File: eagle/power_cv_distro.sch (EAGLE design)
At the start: 54 parts, among them U1 POWER, U10 TLV2372IP, U11 TLV2372IP, U12 TLV2372IP, U13 TLV2372IP, U2 POWER, U3 POWER, U4 POWER, U5 POWER, U6 POWER, U7 POWER, U8 POWER, U9 POWER

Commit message: power dist do-over begins
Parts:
- removed C1, C2, C3, C4: 100n, rcl:C-US025-025X050
- removed C5: 10u, rcl:CPOL-USB45181A
- removed C8: 100n, rcl:C-US050-024X044
- removed JP2, JP3: (no value), pinhead:PINHD-1X8
- removed R1, R10, R13, R14, R2, R5, R6, R7: 1k8, rcl:R-US_0204/2V
- removed R11, R12, R15, R16, R17, R18, R19, R20, R21, R22, R23, R24, R25, R26, R27, R28, R29, R3, R30, R31, R32, R4, R8, R9: 1k, rcl:R-US_0207/7
- removed U$2: FB, adafruit:FB
- added D1, D10, D11, D12, D13, D14, D15, D16, D17, D18, D19, D2, D20, D21, D22, D23, D24, D3, D4, D5, D6, D7, D8, D9: 1N4148DO35-7, TR808clone:1N4148DO35-7
- added X3, X4: (no value), con-molex:22-23-2061
- U10, U11, U12, U13: value TLV2372IP -> POWER; device Texas Instruments_By_element14_Batch_1:TLV2372IP -> eurorack:POWER
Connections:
- removed net N$37: R22.1, U1.GATE
- removed net N$38: R21.1, U1.CV
- removed net N$39: R23.1, U2.GATE
- removed net N$40: R24.1, U2.CV
- removed net N$41: R25.1, U3.GATE
- removed net N$42: R26.1, U3.CV
- removed net N$43: R27.1, U7.GATE
- removed net N$44: R28.1, U7.CV
- removed net N$45: R29.1, U4.GATE
- removed net N$46: R30.1, U4.CV
- removed net N$47: R31.1, U8.GATE
- removed net N$48: R32.1, U8.CV
- removed net VDD: C1.1, C2.1, C3.1, C4.1, C5.+, C8.1, U$2.2, U10.VDD, U11.VDD, U12.VDD, U13.VDD
- net +12V: no longer U$2.1
- net +5V: now also D10.A, D11.A, D12.A, D19.A, D20.A, D21.A, D22.A, D23.A, D24.A, D7.A, D8.A, D9.A, U10.+5V, U11.+5V, U12.+5V, U13.+5V
- net -12V: now also U10.-12V, U11.-12V, U12.-12V, U13.-12V
- net GND: no longer C1.2, C2.2, C3.2, C4.2, C5.-, C8.2, R11.1, R12.1, R15.1, R16.1, R3.1, R4.1, R8.1, R9.1
- net N$1: now also D1.A, X3-1.S; no longer JP2.8, R17.2
- net N$10: now also D4.C, U2.CV; no longer JP3.7, U12.1IN_+
- net N$11: now also D5.C, U3.CV; no longer JP3.6, R27.2
- net N$12: now also D6.C, U7.CV; no longer JP3.5, U12.2IN+
- net N$13: now also D7.C, U5.GATE; no longer JP3.4, R29.2
- net N$14: now also D8.C, U6.GATE; no longer R10.2, R28.2, U12.2OUT
- net N$15: now also D9.C, U1.GATE; no longer JP3.2, R31.2
- net N$16: now also D10.C, U2.GATE; no longer JP3.1, U13.2IN+
- net N$17: now also D11.C, U3.GATE; no longer R1.2, R20.2, U10.2OUT
- net N$18: now also D12.C, U7.GATE; no longer R18.2, R2.2, U10.1OUT
- net N$19: now also D13.A, X4-1.S; no longer R1.1, R3.2, U10.2IN-
- net N$2: now also D2.A, X3-2.S; no longer JP2.7, U10.1IN_+
- net N$20: now also D14.A, X4-2.S; no longer R2.1, R4.2, U10.1IN-
- net N$21: now also D15.A, X4-3.S; no longer R11.2, R7.1, U12.1IN-
- net N$22: now also D17.A, X4-5.S; no longer R24.2, R6.2, U11.2OUT
- net N$23: now also D18.A, X4-6.S; no longer R5.1, R9.2, U11.1IN-
- net N$24: now also D16.A, X4-4.S; no longer R6.1, R8.2, U11.2IN-
- net N$25: now also D13.C, U11.CV; no longer R10.1, R12.2, U12.2IN-
- net N$26: now also D14.C, U12.CV; no longer R21.2, R5.2, U11.1OUT
- net N$27: now also D15.C, U4.CV; no longer R26.2, R7.2, U12.1OUT
- net N$28: now also D16.C, U8.CV; no longer R13.2, R30.2, U13.1OUT
- net N$29: now also D17.C, U10.CV; no longer R14.2, R32.2, U13.2OUT
- net N$3: now also D3.A, X3-3.S; no longer JP2.6, R19.2
- net N$30: now also D18.C, U13.CV; no longer JP3.3, U13.1IN_+
- net N$31: now also D19.C, U11.GATE; no longer R13.1, R15.2, U13.1IN-
- net N$32: now also D20.C, U12.GATE; no longer R14.1, R16.2, U13.2IN-
- net N$33: now also D21.C, U4.GATE; no longer R17.1, U5.GATE
- net N$34: now also D22.C, U8.GATE; no longer R18.1, U5.CV
- net N$35: now also D23.C, U10.GATE; no longer R20.1, U6.CV
- net N$36: now also D24.C, U13.GATE; no longer R19.1, U6.GATE
- net N$4: now also D4.A, X3-4.S; no longer JP2.5, U10.2IN+
- net N$49: now also U10.+12V, U11.+12V, U12.+12V, U13.+12V
- net N$5: now also D5.A, X3-5.S; no longer JP2.4, R22.2
- net N$6: now also D6.A, X3-6.S; no longer JP2.3, U11.1IN_+
- net N$7: now also D1.C, U5.CV; no longer JP2.2, R23.2
- net N$8: now also D2.C, U6.CV; no longer JP2.1, U11.2IN+
- net N$9: now also D3.C, U1.CV; no longer JP3.8, R25.2
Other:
- moved on the sheet: U1, U2, U3, U4, U5, U6, U7, U8, U9

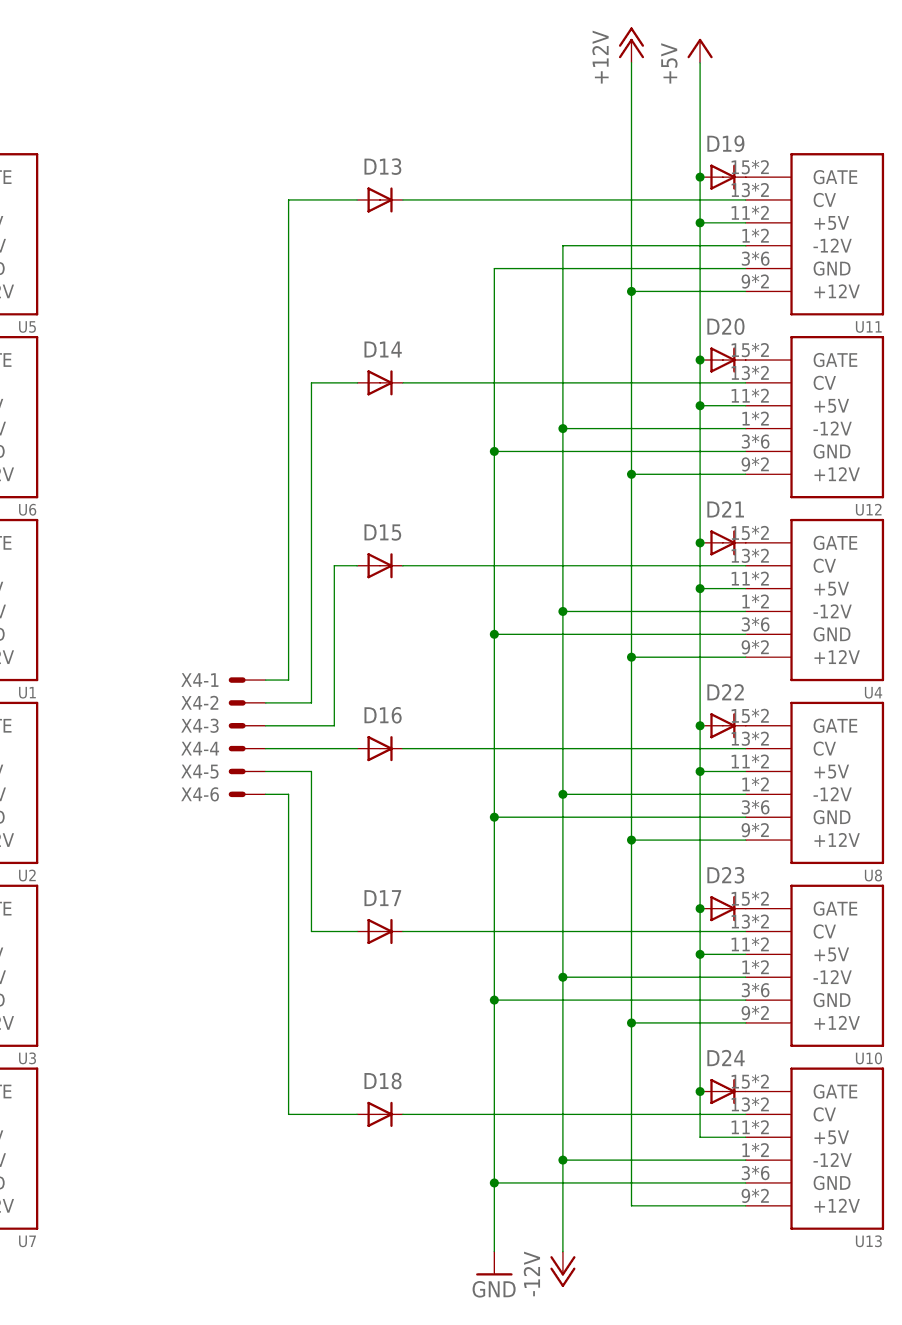
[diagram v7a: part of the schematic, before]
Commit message: power dist to six only
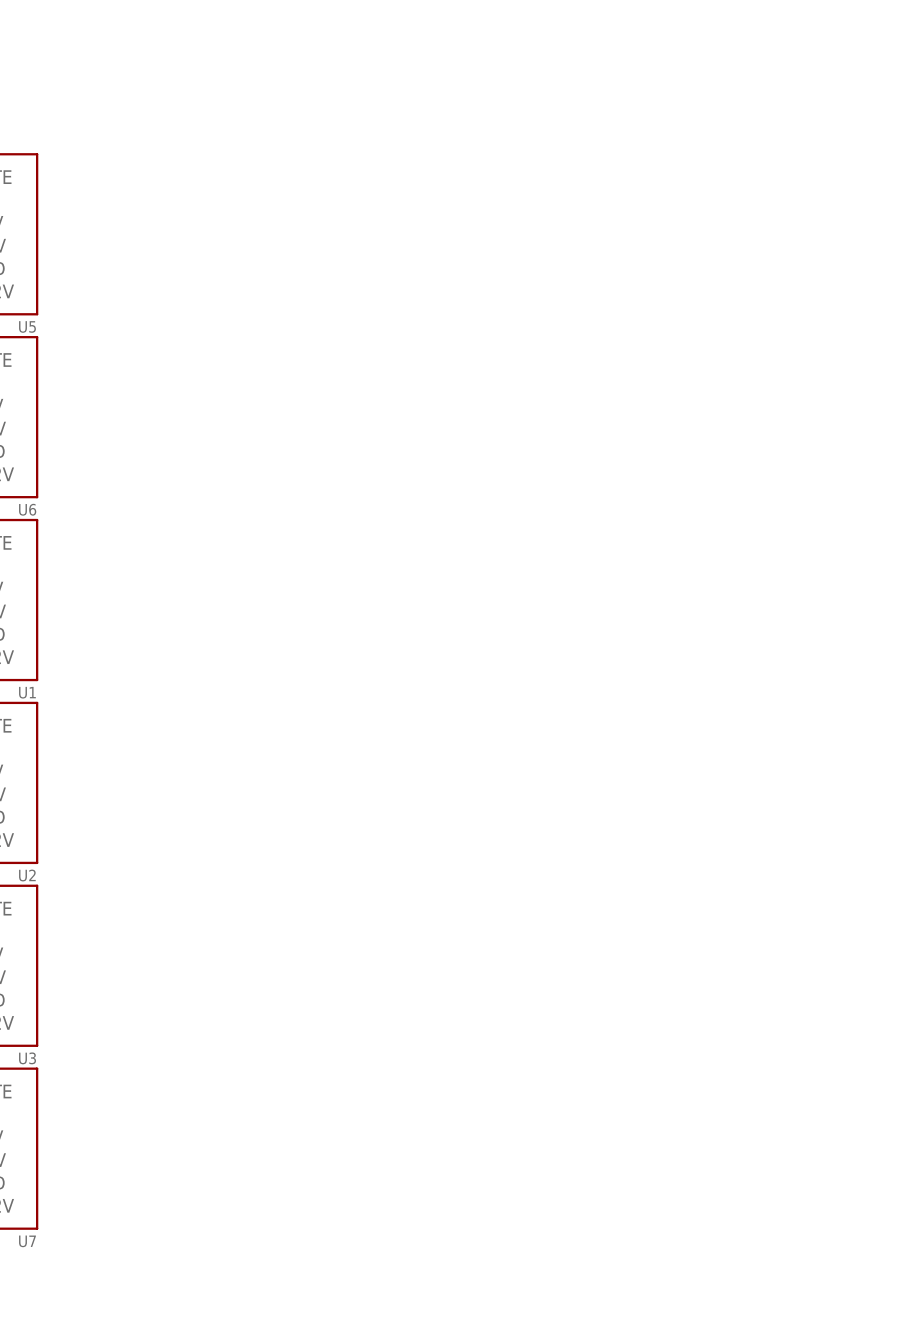
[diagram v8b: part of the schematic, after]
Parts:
- removed D13, D14, D15, D16, D17, D18, D19, D20, D21, D22, D23, D24: 1N4148DO35-7, TR808clone:1N4148DO35-7
- removed U10, U11, U12, U13, U4, U8: POWER, eurorack:POWER
- removed X4: (no value), con-molex:22-23-2061
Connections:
- removed net N$19: D13.A, X4-1.S
- removed net N$20: D14.A, X4-2.S
- removed net N$21: D15.A, X4-3.S
- removed net N$22: D17.A, X4-5.S
- removed net N$23: D18.A, X4-6.S
- removed net N$24: D16.A, X4-4.S
- removed net N$25: D13.C, U11.CV
- removed net N$26: D14.C, U12.CV
- removed net N$27: D15.C, U4.CV
- removed net N$28: D16.C, U8.CV
- removed net N$29: D17.C, U10.CV
- removed net N$30: D18.C, U13.CV
- removed net N$31: D19.C, U11.GATE
- removed net N$32: D20.C, U12.GATE
- removed net N$33: D21.C, U4.GATE
- removed net N$34: D22.C, U8.GATE
- removed net N$35: D23.C, U10.GATE
- removed net N$36: D24.C, U13.GATE
- removed net N$49: U1.+12V, U10.+12V, U11.+12V, U12.+12V, U13.+12V, U2.+12V, U3.+12V, U4.+12V, U5.+12V, U6.+12V, U7.+12V, U8.+12V
- net +12V: now also U1.+12V, U2.+12V, U3.+12V, U5.+12V, U6.+12V, U7.+12V
- net +5V: no longer D19.A, D20.A, D21.A, D22.A, D23.A, D24.A, U10.+5V, U11.+5V, U12.+5V, U13.+5V, U4.+5V, U8.+5V
- net -12V: no longer U10.-12V, U11.-12V, U12.-12V, U13.-12V, U4.-12V, U8.-12V
- net GND: no longer U10.GND, U11.GND, U12.GND, U13.GND, U4.GND, U8.GND
